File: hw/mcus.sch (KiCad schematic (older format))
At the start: 42 parts, among them P15 CONN_1, P16 CONN_1, P18 CONN_1, U13 MPU-9250, U7 STM32F405VG, U8 STM32F303CC, U9 MS5611, X1 8MHz, X2 8MHz

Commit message: HW board revision 1.0
- HMC5983 and MPU6000 replaced by MPU9250 on SPI bus
- added video sync-tip clamping and buffer circuit MAX4090
- added shottky diode D1 as optional alternative for ideal diode circuit LTC4411
- SPI pixel clock generation now also connected to timer output for more fine clock tuning to be possible
- PWM11 and PWM12 signals now switched to PD12 and PD13 to avoid collision of timer usage for sonar echo measurement
- SMT32F4 LEDs moved to more suitable place on the board and blue LED switched to GPIO PC5 (was PE3)
- added micro button
- SWD pads for STM32F3 is now standard 2.54 pitch header
- added SPI flash MICRON N25Q032A13ESC40G
- added pulldown resistors for Q1, Q2
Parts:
- removed P15, P16: CONN_1, testpoint_pad, symbol CONN_1
- added C41: 100nF, c_0603, symbol C
- added P14: CONN_2, ~, symbol CONN_2
- added R62: 39k, r_0603, symbol R
- added SW2: EVQP7A01K, ~, symbol SW_PUSH
- added U10: MICRON N25Q032A13ESC40G, symbol FLASH-SPI-SO8
- U7: value STM32F405VG -> STM32F427VIT6
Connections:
- net +3.3V: now also C41.1, R62.2, U10.3 (~WP), U10.7 (~HOLD), U10.8 (VCC)
- net GND: now also C41.2, SW2.1, U10.4 (GND)
- net PWM11: now also U7.60 (PD13)
- net PWM12: now also U7.59 (PD12)
- net SPI_MISO: now also U10.2 (SO)
- net SPI_MOSI: now also U10.5 (SI)
- net SPI_SCK: now also U10.6 (SCK)
- net at U8.34 (PA13/JTMS/SWDIO): now also P14.2 (PM)
- net at U8.37 (PA14/JTCK/SWCLK): now also P14.1 (P1)
- net at U7.2 (PE3): no longer R54.2
- net at U7.34 (PC5): now also R54.2
- net at U7.77 (PA15-JTDI): now also SW2.2
- net HMC_CS renamed FLASH_CS
- net FLASH_CS: now also R62.1, U10.1 (~CS)
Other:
- note added: "LED_BLUE was here\nin rev. 0.9"
- note added: "Now just for PCB routing\nPWM is on PD12 and PD13"
- note removed: "STM32F427VIT6 is better alternative"
- moved on the sheet: D6, R54

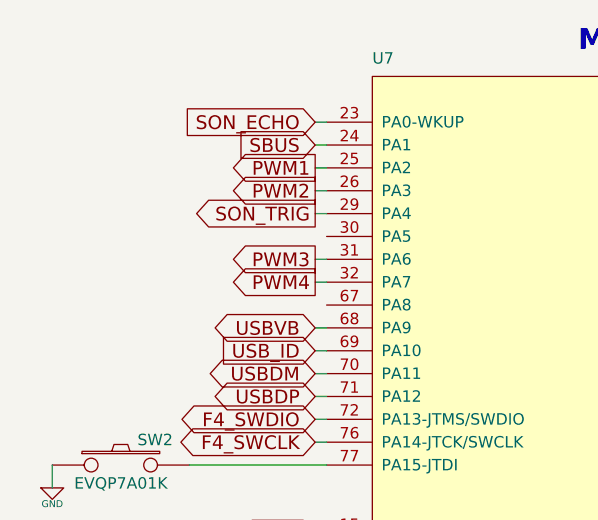
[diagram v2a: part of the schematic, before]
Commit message: hw: SBUS inverting FET replaced by XOR gate (controllable inverter)
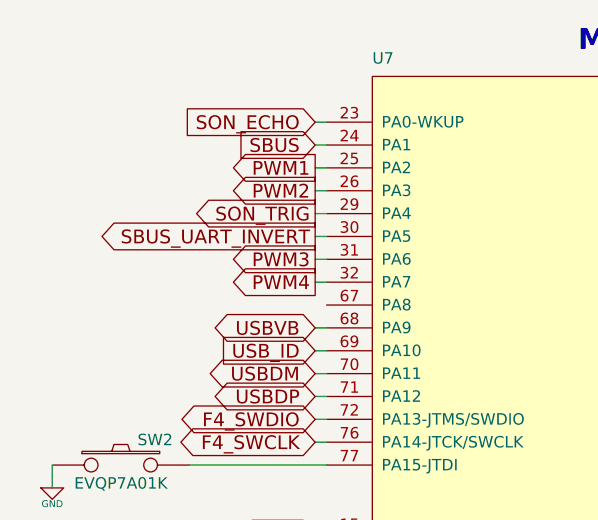
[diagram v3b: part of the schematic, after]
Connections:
- net SBUS_UART_INVERT: now reaches U7.30 (PA5)
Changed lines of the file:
@@
 Sheet 3 3
 Title "DRACO - MCUs sheet"
-Date "18 sep 2014"
+Date "24 sep 2014"
 Rev "1.1"
 Comp "dandys"
@@
 $EndComp
 $Comp
-L GND #PWR66
+L GND #PWR066
 U 1 1 524DA930
 P 1800 7050
-F 0 "#PWR66" H 1800 7050 30  0001 C CNN
+F 0 "#PWR066" H 1800 7050 30  0001 C CNN
 F 1 "GND" H 1800 6980 30  0000 C CNN
 F 2 "" H 1800 7050 60  0000 C CNN
@@
 	4800 7250 4800 6650
 $Comp
-L +3.3V #PWR70
+L +3.3V #PWR067
 U 1 1 524DA98C
 P 5400 6200
-F 0 "#PWR70" H 5400 6160 30  0001 C CNN
+F 0 "#PWR067" H 5400 6160 30  0001 C CNN
 F 1 "+3.3V" H 5400 6310 30  0000 C CNN
 F 2 "" H 5400 6200 60  0000 C CNN
@@
 	4850 5950 5650 5950
 $Comp
-L GND #PWR69
+L GND #PWR068
 U 1 1 524DA9A1
 P 5000 6050
-F 0 "#PWR69" H 5000 6050 30  0001 C CNN
+F 0 "#PWR068" H 5000 6050 30  0001 C CNN
 F 1 "GND" H 5000 5980 30  0000 C CNN
 F 2 "" H 5000 6050 60  0000 C CNN
@@
 Connection ~ 5650 5250
 $Comp
-L +3.3V #PWR72
+L +3.3V #PWR069
 U 1 1 524DA9E3
 P 6300 5200
-F 0 "#PWR72" H 6300 5160 30  0001 C CNN
+F 0 "#PWR069" H 6300 5160 30  0001 C CNN
 F 1 "+3.3V" H 6300 5310 30  0000 C CNN
 F 2 "" H 6300 5200 60  0000 C CNN
@@
 Connection ~ 8250 1250
 $Comp
-L +3.3V #PWR75
+L +3.3V #PWR070
 U 1 1 524DAA14
 P 7750 1300
-F 0 "#PWR75" H 7750 1260 30  0001 C CNN
+F 0 "#PWR070" H 7750 1260 30  0001 C CNN
 F 1 "+3.3V" H 7750 1410 30  0000 C CNN
 F 2 "" H 7750 1300 60  0000 C CNN
@@
 Connection ~ 8550 850
 $Comp
-L GND #PWR74
+L GND #PWR071
 U 1 1 524DAA1F
 P 7750 1000
-F 0 "#PWR74" H 7750 1000 30  0001 C CNN
+F 0 "#PWR071" H 7750 1000 30  0001 C CNN
 F 1 "GND" H 7750 930 30  0000 C CNN
 F 2 "" H 7750 1000 60  0000 C CNN
@@
 Connection ~ 8350 5200
 $Comp
-L GND #PWR76
+L GND #PWR072
 U 1 1 524DAA4C
 P 8350 5300
-F 0 "#PWR76" H 8350 5300 30  0001 C CNN
+F 0 "#PWR072" H 8350 5300 30  0001 C CNN
 F 1 "GND" H 8350 5230 30  0000 C CNN
 F 2 "" H 8350 5300 60  0000 C CNN
@@
 	1800 2850 1850 2850
 $Comp
-L GND #PWR68
+L GND #PWR073
 U 1 1 524DAA81
 P 4600 1250
-F 0 "#PWR68" H 4600 1250 30  0001 C CNN
+F 0 "#PWR073" H 4600 1250 30  0001 C CNN
 F 1 "GND" H 4600 1180 30  0000 C CNN
 F 2 "" H 4600 1250 60  0000 C CNN
@@
 	4550 1250 4600 1250
 $Comp
-L GND #PWR79
+L GND #PWR074
 U 1 1 524DAA8F
 P 10250 4150
-F 0 "#PWR79" H 10250 4150 30  0001 C CNN
+F 0 "#PWR074" H 10250 4150 30  0001 C CNN
 F 1 "GND" H 10250 4080 30  0000 C CNN
 F 2 "" H 10250 4150 60  0000 C CNN
@@
 	1800 2050 1850 2050
 $Comp
-L GND #PWR67
+L GND #PWR075
 U 1 1 524DF976
 P 3250 7300
-F 0 "#PWR67" H 3250 7300 30  0001 C CNN
+F 0 "#PWR075" H 3250 7300 30  0001 C CNN
 F 1 "GND" H 3250 7230 30  0000 C CNN
 F 2 "" H 3250 7300 60  0000 C CNN
@@
 	5800 4400 5800 5050
 $Comp
-L GND #PWR71
+L GND #PWR076
 U 1 1 52509365
 P 5800 5050
-F 0 "#PWR71" H 5800 5050 30  0001 C CNN
+F 0 "#PWR076" H 5800 5050 30  0001 C CNN
 F 1 "GND" H 5800 4980 30  0000 C CNN
 F 2 "" H 5800 5050 60  0000 C CNN
@@
 	10950 4300 10950 4950
 $Comp
-L GND #PWR80
+L GND #PWR077
 U 1 1 52509B41
 P 10950 4950
-F 0 "#PWR80" H 10950 4950 30  0001 C CNN
+F 0 "#PWR077" H 10950 4950 30  0001 C CNN
 F 1 "GND" H 10950 4880 30  0000 C CNN
 F 2 "" H 10950 4950 60  0000 C CNN
@@
 F3_INT
 $Comp
-L GND #PWR85
+L GND #PWR078
 U 1 1 525A6131
 P 13700 4850
-F 0 "#PWR85" H 13700 4850 30  0001 C CNN
+F 0 "#PWR078" H 13700 4850 30  0001 C CNN
 F 1 "GND" H 13700 4780 30  0000 C CNN
 F 2 "" H 13700 4850 60  0000 C CNN
@@
 	8300 7450 8350 7450
 $Comp
-L +3.3VADC #PWR77
+L +3.3VADC #PWR079
 U 1 1 525ABDC4
 P 9200 7000
-F 0 "#PWR77" H 9200 7120 20  0001 C CNN
+F 0 "#PWR079" H 9200 7120 20  0001 C CNN
 F 1 "+3.3VADC" H 9200 7090 30  0000 C CNN
 F 2 "" H 9200 7000 60  0000 C CNN
@@
 $EndComp
 $Comp
-L GND #PWR64
+L GND #PWR080
 U 1 1 525AC825
 P 1050 3800
-F 0 "#PWR64" H 1050 3800 30  0001 C CNN
+F 0 "#PWR080" H 1050 3800 30  0001 C CNN
 F 1 "GND" H 1050 3730 30  0000 C CNN
 F 2 "" H 1050 3800 60  0000 C CNN
@@
 $EndComp
 $Comp
-L GND #PWR65
+L GND #PWR081
 U 1 1 525B2104
 P 1050 5800
-F 0 "#PWR65" H 1050 5800 30  0001 C CNN
+F 0 "#PWR081" H 1050 5800 30  0001 C CNN
 F 1 "GND" H 1050 5730 30  0000 C CNN
 F 2 "" H 1050 5800 60  0000 C CNN
@@
 	1050 5350 1300 5350
 $Comp
-L GND #PWR78
+L GND #PWR082
 U 1 1 525B4514
 P 9200 8400
-F 0 "#PWR78" H 9200 8400 30  0001 C CNN
+F 0 "#PWR082" H 9200 8400 30  0001 C CNN
 F 1 "GND" H 9200 8330 30  0000 C CNN
 F 2 "" H 9200 8400 60  0000 C CNN
@@
 Connection ~ 7650 7850
 $Comp
-L +3.3V #PWR73
+L +3.3V #PWR083
 U 1 1 5276BBE1
 P 7650 6750
-F 0 "#PWR73" H 7650 6710 30  0001 C CNN
+F 0 "#PWR083" H 7650 6710 30  0001 C CNN
 F 1 "+3.3V" H 7650 6860 30  0000 C CNN
 F 2 "" H 7650 6750 60  0000 C CNN
@@
 Connection ~ 15000 2400
 $Comp
-L GND #PWR83
+L GND #PWR084
 U 1 1 52FFF2C2
 P 12750 3800
-F 0 "#PWR83" H 12750 3800 30  0001 C CNN
+F 0 "#PWR084" H 12750 3800 30  0001 C CNN
 F 1 "GND" H 12750 3730 30  0000 C CNN
 F 2 "" H 12750 3800 60  0000 C CNN
@@
 	12750 3750 12850 3750
 $Comp
-L +3.3V #PWR84
+L +3.3V #PWR085
 U 1 1 52FFF4C5
 P 13700 1950
-F 0 "#PWR84" H 13700 1910 30  0001 C CNN
+F 0 "#PWR085" H 13700 1910 30  0001 C CNN
 F 1 "+3.3V" H 13700 2060 30  0000 C CNN
 F 2 "" H 13700 1950 60  0000 C CNN
@@
 	13700 2000 13700 1950
 $Comp
-L +3.3V #PWR82
+L +3.3V #PWR086
 U 1 1 52FFF5C4
 P 12750 3600
-F 0 "#PWR82" H 12750 3560 30  0001 C CNN
+F 0 "#PWR086" H 12750 3560 30  0001 C CNN
 F 1 "+3.3V" H 12750 3710 30  0000 C CNN
 F 2 "" H 12750 3600 60  0000 C CNN
@@
 $EndComp
 $Comp
-L GND #PWR86
+L GND #PWR087
 U 1 1 530122C5
 P 13850 6300
-F 0 "#PWR86" H 13850 6300 30  0001 C CNN
+F 0 "#PWR087" H 13850 6300 30  0001 C CNN
 F 1 "GND" H 13850 6230 30  0000 C CNN
 F 2 "" H 13850 6300 60  0000 C CNN
@@
 Connection ~ 14400 5750
 $Comp
-L +3.3V #PWR87
+L +3.3V #PWR088
 U 1 1 5301275E
 P 14050 5500
-F 0 "#PWR87" H 14050 5460 30  0001 C CNN
+F 0 "#PWR088" H 14050 5460 30  0001 C CNN
 F 1 "+3.3V" H 14050 5610 30  0000 C CNN
 F 2 "" H 14050 5500 60  0000 C CNN
@@
 Connection ~ 12500 5950
 $Comp
-L +3.3V #PWR81
+L +3.3V #PWR089
 U 1 1 53013135
 P 12500 5200
-F 0 "#PWR81" H 12500 5160 30  0001 C CNN
+F 0 "#PWR089" H 12500 5160 30  0001 C CNN
 F 1 "+3.3V" H 12500 5310 30  0000 C CNN
 F 2 "" H 12500 5200 60  0000 C CNN
@@
 	1250 2550 1850 2550
 $Comp
-L GND #PWR63
+L GND #PWR090
 U 1 1 530283DD
 P 650 2650
-F 0 "#PWR63" H 650 2650 30  0001 C CNN
+F 0 "#PWR090" H 650 2650 30  0001 C CNN
 F 1 "GND" H 650 2580 30  0000 C CNN
 F 2 "" H 650 2650 60  0000 C CNN
@@
 Wire Wire Line
 	5900 3400 5900 3200
+Text GLabel 1800 1550 0    60   Output ~ 0
+SBUS_UART_INVERT
+Wire Wire Line
+	1800 1550 1850 1550
 $EndSCHEMATC
